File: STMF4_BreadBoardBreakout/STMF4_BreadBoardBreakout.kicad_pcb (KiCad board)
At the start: 2 copper layers, 84.1 x 127.7 mm, 48 parts, among them IC1 SGM2019-ADJYN5G-TR, J1 USART1, J10 PORT D, J11 PORT E, J2 USB_B_Micro, J3 USART2, J4 SWD, J5 I2C3, J6 SPI1, J7 PORT A, J8 PORT B, J9 PORT C, U1 STM32F446VETx, Y1 Crystal

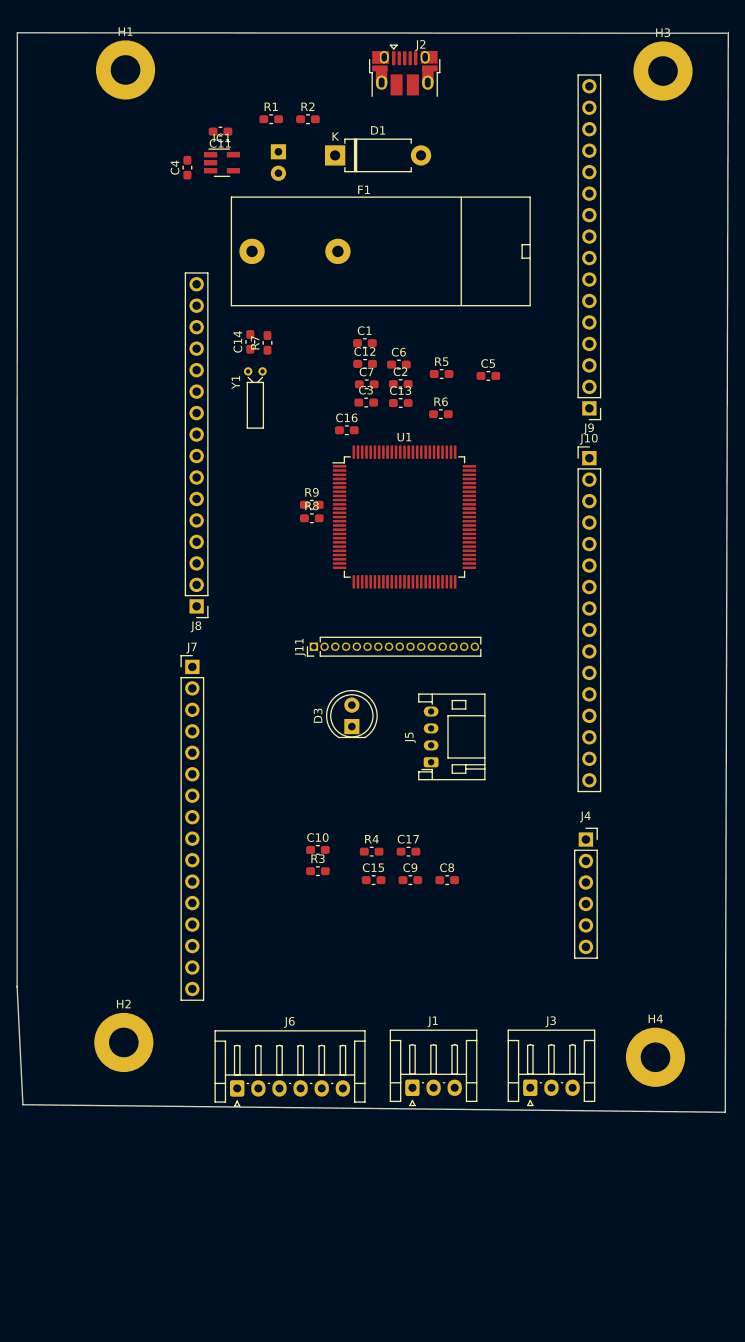
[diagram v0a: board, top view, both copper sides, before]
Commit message: rough component placement, change to smd
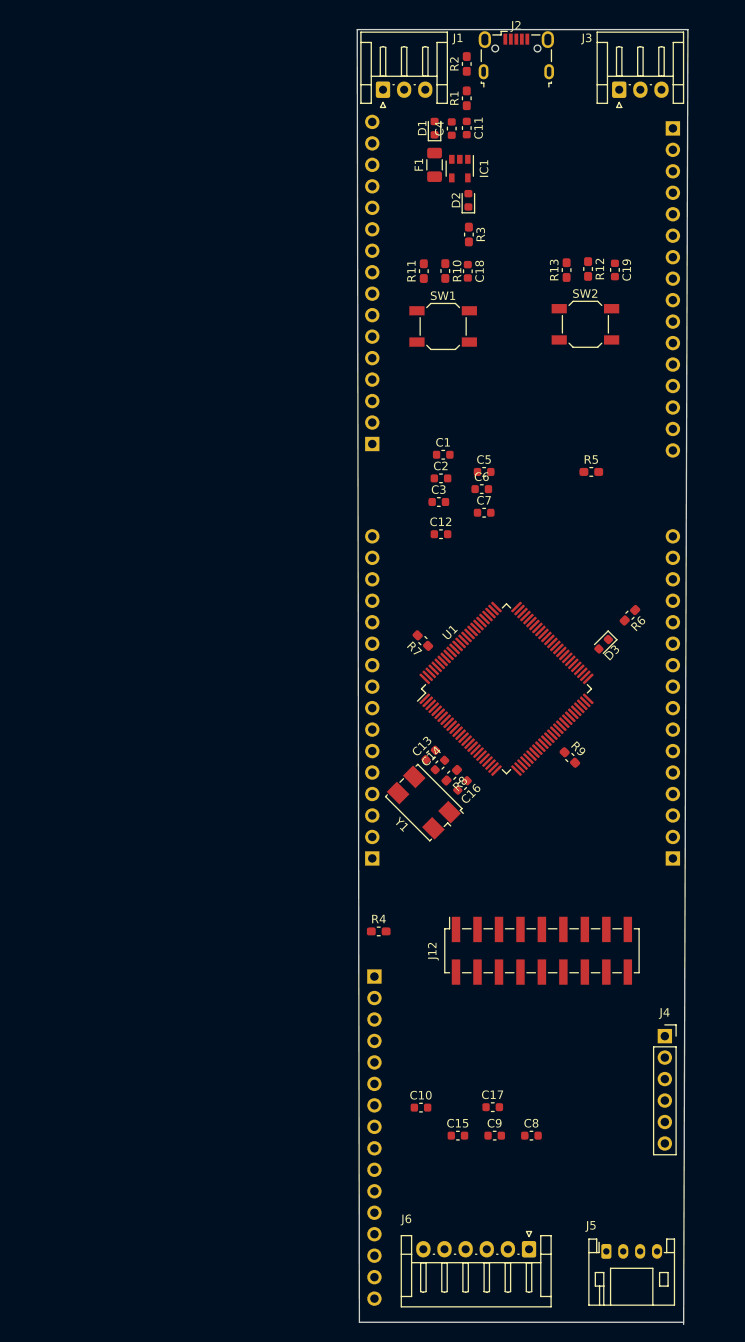
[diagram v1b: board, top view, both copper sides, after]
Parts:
- removed H1, H2, H3, H4: MountingHole_Pad, MountingHole:MountingHole_3.5mm_Pad
- added C18: 10uF, Capacitor_SMD:C_0603_1608Metric, F.Cu at (68.5, 40.8)
- added C19: 10uF, Capacitor_SMD:C_0603_1608Metric, F.Cu at (85.9, 40.6)
- added J12: DCMI SPI CAM, Connector_PinSocket_2.54mm:PinSocket_2x09_P2.54mm_Vertical_SMD, F.Cu at (77.2, 121.2)
- added R10: 10k, Resistor_SMD:R_0603_1608Metric_Pad1.05x0.95mm_HandSolder, F.Cu at (65.8, 40.8)
- added R11: 1k, Resistor_SMD:R_0603_1608Metric_Pad1.05x0.95mm_HandSolder, F.Cu at (63.2, 40.8)
- added R12: 10k, Resistor_SMD:R_0603_1608Metric_Pad1.05x0.95mm_HandSolder, F.Cu at (82.7, 40.5)
- added R13: 1k, Resistor_SMD:R_0603_1608Metric_Pad1.05x0.95mm_HandSolder, F.Cu at (80.1, 40.6)
- added SW1: BTN_NRST, Button_Switch_SMD:SW_SPST_SKQG_WithStem, F.Cu at (65.5, 47.3)
- added SW2: BTN_UTIL1, Button_Switch_SMD:SW_SPST_SKQG_WithStem, F.Cu at (82.4, 47.1)
- C1, C10, C11, C12, C13, C14, C15, C16, C17, C2, C3, C4, C5, C6, C7, C8, C9: footprint Capacitor_SMD:C_0603_1608Metric_Pad1.05x0.95mm_HandSolder -> Capacitor_SMD:C_0603_1608Metric
- D1: footprint Diode_THT:D_DO-15_P10.16mm_Horizontal -> Diode_SMD:D_0603_1608Metric
- D2: footprint LED_THT:LED_D5.0mm -> Diode_SMD:D_0603_1608Metric; moved to F.Cu
- D3: footprint LED_THT:LED_D5.0mm -> Diode_SMD:D_0603_1608Metric
- F1: footprint Fuse:Fuseholder_Cylinder-5x20mm_Bulgin_FX0457_Horizontal_Closed -> Fuse:Fuse_1206_3216Metric
- IC1: footprint Package_TO_SOT_SMD:SOT-23-5_HandSoldering -> Package_TO_SOT_SMD:SOT-23-5
- J10, J7, J8, J9: moved to B.Cu
- J11: footprint Connector_PinHeader_1.27mm:PinHeader_1x16_P1.27mm_Vertical -> Connector_PinHeader_2.54mm:PinHeader_1x16_P2.54mm_Vertical; moved to B.Cu
- J2: footprint Connector_USB:USB_Micro-B_Amphenol_10103594-0001LF_Horizontal -> Connector_USB:USB_Micro-B_Wuerth_629105150521
- Y1: footprint Crystal:Crystal_DS15_D1.5mm_L5.0mm_Horizontal -> Crystal:Crystal_SMD_7050-4Pin_7.0x5.0mm
- moved J3 118.5 mm to (86.4, 19.3)
- moved J1 118.1 mm to (58.4, 19.3)
- moved R3 77.4 mm to (68.6, 36.4), turned to 270 degrees
- moved J11 74.6 mm to (92.7, 23.9), turned to 180 degrees
- moved J5 61.5 mm to (84.8, 156.7), turned to 0 degrees
- moved Y1 55.1 mm to (63.2, 103.6), turned to 135 degrees
- moved C14 54.8 mm to (65.2, 99.2), turned to 45 degrees
- moved J9 54.1 mm to (92.7, 110.2), turned to 0 degrees
- moved J8 48.6 mm to (57.4, 124.2)
- moved C16 44.2 mm to (67.8, 101.6), turned to 225 degrees
- moved R9 42.7 mm to (80.5, 98.3), turned to 315 degrees
- moved C13 41.8 mm to (64.1, 98.0), turned to 45 degrees
- moved R7 39.7 mm to (63.1, 84.5), turned to 135 degrees
- moved J6 39.4 mm to (75.7, 156.5), turned to 180 degrees
- moved R8 34.6 mm to (66.5, 100.4), turned to 225 degrees
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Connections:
- R9 pad 1: BOOT0 -> BOOT1
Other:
- board size 84.1 x 127.7 mm -> 39.1 x 153.2 mm

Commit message: reduce size in pcb, fix second sheet, main routing finished
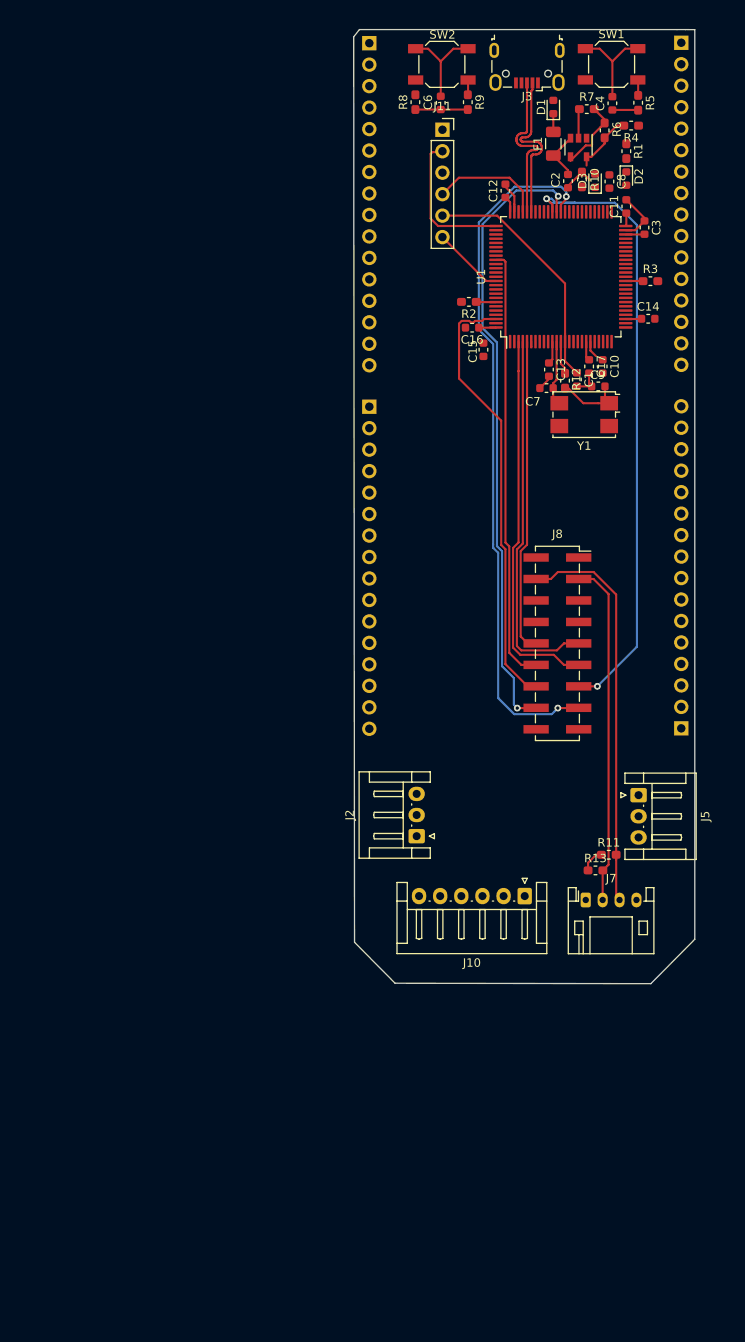
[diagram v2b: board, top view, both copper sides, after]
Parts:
- removed the C14 at (65.2, 99.2)
- removed C18, C19: 10uF, Capacitor_SMD:C_0603_1608Metric
- removed J1: USART1, Connector_JST:JST_EH_S3B-EH_1x03_P2.50mm_Horizontal
- C12: value 1nF -> 100nF
- C13: value 10uF -> 100nF
- C15: value 2.2uF -> 100nF
- C17: value 2.2uF -> 10u
- C2: value 100nF -> 1u
- C3: value 100nF -> 2.2uF
- C4, C9: value 1u -> 10uF
- C6, C7: value 100nF -> 10uF
- C8: value 10u -> 1u
- J10: value PORT D -> SPI1; footprint Connector_PinHeader_2.54mm:PinHeader_1x16_P2.54mm_Vertical -> Connector_JST:JST_EH_S6B-EH_1x06_P2.50mm_Horizontal; moved to F.Cu
- J11: value PORT E -> SWD; footprint Connector_PinHeader_2.54mm:PinHeader_1x16_P2.54mm_Vertical -> Connector_PinSocket_2.54mm:PinSocket_1x06_P2.54mm_Vertical; moved to F.Cu
- J12: value DCMI SPI CAM -> PORT E; footprint Connector_PinSocket_2.54mm:PinSocket_2x09_P2.54mm_Vertical_SMD -> Connector_PinHeader_2.54mm:PinHeader_1x16_P2.54mm_Vertical; moved to B.Cu
- J2: value USB_B_Micro -> USART1; footprint Connector_USB:USB_Micro-B_Wuerth_629105150521 -> Connector_JST:JST_EH_S3B-EH_1x03_P2.50mm_Horizontal
- J3: value USART2 -> USB_B_Micro; footprint Connector_JST:JST_EH_S3B-EH_1x03_P2.50mm_Horizontal -> Connector_USB:USB_Micro-B_Wuerth_629105150521
- J4: value SWD -> PORT B; footprint Connector_PinSocket_2.54mm:PinSocket_1x06_P2.54mm_Vertical -> Connector_PinHeader_2.54mm:PinHeader_1x16_P2.54mm_Vertical; moved to B.Cu
- J5: value I2C3 -> USART2; footprint Connector_JST:JST_PH_S4B-PH-K_1x04_P2.00mm_Horizontal -> Connector_JST:JST_EH_S3B-EH_1x03_P2.50mm_Horizontal
- J6: value SPI1 -> PORT C; footprint Connector_JST:JST_EH_S6B-EH_1x06_P2.50mm_Horizontal -> Connector_PinHeader_2.54mm:PinHeader_1x16_P2.54mm_Vertical; moved to B.Cu
- J7: value PORT A -> I2C3; footprint Connector_PinHeader_2.54mm:PinHeader_1x16_P2.54mm_Vertical -> Connector_JST:JST_PH_S4B-PH-K_1x04_P2.00mm_Horizontal; moved to F.Cu
- J8: value PORT B -> DCMI SPI CAM; footprint Connector_PinHeader_2.54mm:PinHeader_1x16_P2.54mm_Vertical -> Connector_PinSocket_2.54mm:PinSocket_2x09_P2.54mm_Vertical_SMD; moved to F.Cu
- J9: value PORT C -> PORT D
- R1: value 73.2k -> 2.2k
- R10: value 10k -> 2.2k
- R11, R13: value 1k -> 2.2k
- R2: value 42.2k -> 10k
- R3, R4: value 2.2k -> 10k
- R5: value 2.2k -> 1k
- R6: value 2.2k -> 73.2k
- R7: value 10k -> 42.2k
- R9: value 10k -> 1k
- moved J4 122.5 mm to (56.8, 13.8), turned to 180 degrees
- moved C8 113.2 mm to (85.2, 30.2), turned to 270 degrees
- moved J6 101.4 mm to (56.8, 56.8)
- moved R4 99.9 mm to (87.8, 23.6), turned to 180 degrees
- moved J9 96.5 mm to (93.7, 13.8), turned to 180 degrees
- moved J2 93.1 mm to (62.4, 107.6), turned to 90 degrees
- moved C15 93.0 mm to (70.3, 50.1), turned to 270 degrees
- moved C10 90.3 mm to (84.4, 52.0), turned to 270 degrees
- moved C9 89.5 mm to (83.9, 54.4), turned to 180 degrees
- moved C17 88.4 mm to (82.8, 52.0), turned to 270 degrees
- moved R8 79.7 mm to (62.2, 20.8), turned to 90 degrees
- moved R9 78.5 mm to (68.5, 20.8), turned to 270 degrees
- moved R11 72.4 mm to (85.1, 109.8), turned to 0 degrees
- moved R13 71.1 mm to (83.5, 111.7), turned to 0 degrees
- moved R7 65.8 mm to (82.5, 21.6), turned to 180 degrees
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- renumbered C5 to C14
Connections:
- C1 pad 1: +3.3VA -> NRST
- C10 pad 1: +3.3VA -> +3.3V
- C11 pad 1: +3.3VA -> +3.3V
- C12 pad 1: +3.3VA -> +3.3V
- C13 pad 1: HSE_IN -> +3.3V
- C14 pad 1: +3.3VA -> +3.3V
- C15 pad 1: vCAP_1 -> +3.3V
- C16 pad 1: NRST -> +3.3V
- C17 pad 1: vCAP_1 -> +3.3V
- C2 pad 1: +3.3VA -> Net-(C2-Pad1)
- C3 pad 1: +3.3VA -> vCAP_1
- C6 pad 1: +3.3VA -> Net-(C6-Pad1)
- C7 pad 1: +3.3VA -> HSE_IN
- C8 pad 1: +3.3VA -> +3.3V
- C9 pad 1: +3.3VA -> Net-(C9-Pad1)
- D2 pad 2: +3.3VA -> LED_STATUS
- D3 pad 2: LED_STATUS -> +3.3V
- F1 pad 1: Net-(C4-Pad1) -> Net-(C2-Pad1)
- IC1 pad 1: Net-(C4-Pad1) -> Net-(C2-Pad1)
- IC1 pad 3: Net-(C4-Pad1) -> Net-(C2-Pad1)
- IC1 pad 5: +3.3VA -> +3.3V
- J10 pad 1: CAN1_RX -> +3V3
- J10 pad 2: CAN1_TX -> (no net)
- J10 pad 3: PD2 -> (no net)
- J10 pad 4: PD3 -> (no net)
- J10 pad 5: PD4 -> (no net)
- J10 pad 6: PD5 -> GND
- J11 pad 1: PE0 -> +3V3
- J11 pad 2: PE1 -> SYS_SWCLK
- J11 pad 3: PE2 -> GND
- J11 pad 4: PE3 -> SYS_SWDIO
- J11 pad 5: PE4 -> NRST
- J11 pad 6: PE5 -> SYS_SWO
- J12 pad 1: +3.3VA -> PE0
- J12 pad 10: D7 -> PE9
- J12 pad 11: D4 -> PE10
- J12 pad 12: D5 -> PE11
- J12 pad 13: D2 -> PE12
- J12 pad 14: D3 -> PE13
- J12 pad 15: D0 -> PE14
- J12 pad 16: D1 -> PE15
- J12 pad 2: GND -> DCMI_D3
- J12 pad 3: I2C3_SDA -> PE2
- J12 pad 4: I2C3_SCL -> PE3
- J12 pad 5: HS -> DCMI_D4
- J12 pad 6: VS -> DCMI_D6
- J12 pad 7: MCLK -> DCMI_D7
- J12 pad 8: PCLK -> PE7
- J12 pad 9: D6 -> PE8
- J2 pad 1: +5V -> (no net)
- J2 pad 2: USB_FS_DM -> (no net)
- J2 pad 3: USB_FS_DP -> GND
- J3 pad 1: USART2_TX -> +5V
- J3 pad 2: USART2_RX -> USB_FS_-
- J3 pad 3: GND -> USB_FS_+
- J4 pad 1: +3.3VA -> PB0
- J4 pad 2: SWDCLK -> PB1
- J4 pad 3: GND -> BOOT1
- J4 pad 4: SWDIO -> (no net)
- J4 pad 5: NRST -> PB4
- J4 pad 6: SWO -> PB5
- J5 pad 1: +3.3VA -> (no net)
- J5 pad 2: I2C3_SDA -> (no net)
- J5 pad 3: I2C3_SCL -> GND
- J6 pad 1: +3.3VA -> PC0
- J6 pad 2: SPI1_MIS0 -> PC1
- J6 pad 3: SPI1_SCK -> PC2
- J6 pad 4: SPI1_MOSI -> PC3
- J6 pad 5: SPI1_RST -> PC4
- J6 pad 6: GND -> PC5
- J7 pad 1: PA0 -> +3V3
- J7 pad 2: PA1 -> I2C3_SDA
- J7 pad 3: USART2_TX -> I2C3_SCL
- J7 pad 4: USART2_RX -> GND
- J8 pad 1: PB0 -> +3V3
- J8 pad 10: PB9 -> DCMI_D7
- J8 pad 11: PB10 -> DCMI_D4
- J8 pad 12: PB12 -> DCMI_D5
- J8 pad 13: PB13 -> DCMI_D2
- J8 pad 14: PB14 -> DCMI_D3
- J8 pad 15: LED_STATUS -> DCMI_D0
- J8 pad 16: Net-(J8-Pad16) -> DCMI_D1
- J8 pad 2: PB1 -> GND
- J8 pad 3: BOOT1 -> I2C3_SDA
- J8 pad 4: SWDIO -> I2C3_SCL
- J8 pad 5: PB4 -> GND
- J8 pad 6: PB5 -> GND
- J8 pad 7: PB6 -> GND
- J8 pad 8: PB7 -> (no net)
- J8 pad 9: PB8 -> DCMI_D6
- J9 pad 1: PC0 -> (no net)
- J9 pad 10: I2C3_SDA -> PD9
- J9 pad 11: PC10 -> PD10
- J9 pad 12: PC11 -> PD11
- J9 pad 13: PC12 -> PD12
- J9 pad 14: PC13 -> PD13
- J9 pad 15: PC14 -> PD14
- J9 pad 16: PC15 -> PD15
- J9 pad 2: PC1 -> (no net)
- J9 pad 3: PC2 -> DCMI_D5
- J9 pad 4: PC3 -> (no net)
- J9 pad 5: PC4 -> PD4
- J9 pad 6: PC5 -> PD5
- J9 pad 7: PC6 -> PD6
- J9 pad 8: PC7 -> PD7
- J9 pad 9: PC8 -> PD8
- R1 pad 1: +3.3VA -> GND
- R1 pad 2: Net-(IC1-Pad4) -> Net-(D2-Pad1)
- R10 pad 1: Net-(C18-Pad1) -> Net-(D3-Pad1)
- R10 pad 2: +3.3VA -> GND
- R11 pad 1: Net-(R11-Pad1) -> +3.3V
- R11 pad 2: Net-(C18-Pad1) -> I2C3_SCL
- R12 pad 1: Net-(C19-Pad1) -> HSE_OUT
- R12 pad 2: +3.3VA -> Net-(C9-Pad1)
- R13 pad 1: Net-(R13-Pad1) -> +3.3V
- R13 pad 2: Net-(C19-Pad1) -> I2C3_SDA
- R2 pad 1: Net-(IC1-Pad4) -> BOOT0
- R3 pad 1: Net-(D2-Pad1) -> BOOT1
- R4 pad 1: +3.3VA -> Net-(C4-Pad1)
- R4 pad 2: I2C3_SCL -> +3.3V
- R5 pad 1: +3.3VA -> Net-(R5-Pad1)
- R5 pad 2: I2C3_SDA -> Net-(C4-Pad1)
- R6 pad 1: GND -> +3.3V
- R6 pad 2: Net-(D3-Pad1) -> Net-(IC1-Pad4)
- R7 pad 1: BOOT0 -> Net-(IC1-Pad4)
- R8 pad 1: HSE_OUT -> Net-(C6-Pad1)
- R8 pad 2: Net-(C14-Pad1) -> +3.3V
- R9 pad 1: BOOT1 -> Net-(R9-Pad1)
- R9 pad 2: GND -> Net-(C6-Pad1)
- SW1 pad 1: Net-(R11-Pad1) -> Net-(R5-Pad1)
- SW2 pad 1: Net-(R13-Pad1) -> Net-(R9-Pad1)
- U1 pad 100: /3.3V -> +3.3V
- U1 pad 11: /3.3V -> +3.3V
- U1 pad 19: /3.3V -> +3.3V
- U1 pad 21: Net-(U1-Pad21) -> (no net)
- U1 pad 22: Net-(U1-Pad22) -> +3.3V
- U1 pad 23: PA0 -> (no net)
- U1 pad 24: PA1 -> (no net)
- U1 pad 25: USART2_TX -> (no net)
- U1 pad 26: USART2_RX -> (no net)
- U1 pad 28: /3.3V -> +3.3V
- U1 pad 29: PA4 -> (no net)
- U1 pad 3: PE4 -> DCMI_D4
- U1 pad 30: SPI1_SCK -> (no net)
- U1 pad 31: SPI1_MIS0 -> (no net)
- U1 pad 32: SPI1_MOSI -> (no net)
- U1 pad 4: PE5 -> DCMI_D6
- U1 pad 5: PE6 -> DCMI_D7
- U1 pad 50: /3.3V -> +3.3V
- U1 pad 6: /3.3V -> +3.3V
- U1 pad 63: PC6 -> DCMI_D0
- U1 pad 64: PC7 -> DCMI_D1
- U1 pad 65: PC8 -> DCMI_D2
- U1 pad 66: I2C3_SDA -> (no net)
- U1 pad 67: I2C3_SCL -> (no net)
- U1 pad 68: USART1_TX -> (no net)
- U1 pad 69: USART1_RX -> (no net)
- U1 pad 70: USB_FS_DM -> USB_FS_-
- U1 pad 71: USB_FS_DP -> USB_FS_+
- U1 pad 72: SWDIO -> SYS_SWDIO
- U1 pad 73: vCAP_2 -> (no net)
- U1 pad 75: /3.3V -> +3.3V
- U1 pad 76: SWCLK -> SYS_SWCLK
- U1 pad 77: PA15 -> (no net)
- U1 pad 81: CAN1_RX -> (no net)
- U1 pad 82: CAN1_TX -> (no net)
- U1 pad 83: PD2 -> (no net)
- U1 pad 84: PD3 -> DCMI_D5
- U1 pad 89: SWDIO -> SYS_SWO
- U1 pad 92: PB6 -> (no net)
- U1 pad 98: PE1 -> DCMI_D3
- Y1 pad 1: Net-(C14-Pad1) -> Net-(C9-Pad1)
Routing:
- net DCMI_D0: track 0.00 -> 82.8 mm, vias 0 -> 2
- net DCMI_D2: track 0.00 -> 76.3 mm, vias 0 -> 2
- net DCMI_D1: track 0.00 -> 74.1 mm, vias 0 -> 2
- net DCMI_D3: track 0.00 -> 52.0 mm
- net DCMI_D5: track 0.00 -> 51.4 mm
- net I2C3_SCL: track 0.00 -> 47.8 mm
- net GND: track 0.00 -> 47.7 mm
- net DCMI_D4: track 0.00 -> 45.1 mm
- net DCMI_D6: track 0.00 -> 44.2 mm
- net I2C3_SDA: track 0.00 -> 40.7 mm
- net DCMI_D7: track 0.00 -> 37.3 mm
- net NRST: track 0.00 -> 29.0 mm
- net +3.3V: track 0.00 -> 23.2 mm
- net USB_FS_-: track 0.00 -> 19.1 mm
- net USB_FS_+: track 0.00 -> 19.0 mm
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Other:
- board size 39.1 x 153.2 mm -> 40.3 x 112.9 mm
- board text added: "CAMERA"
